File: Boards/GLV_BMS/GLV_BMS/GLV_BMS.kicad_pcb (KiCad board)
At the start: 2 copper layers, 44 parts, among them J1 CONN_02X03, J2 CONN_02X03, J3 MM_F_RA_20, U1 MCP2561-E_SN, U101 TPS560430YF, U2 ATMEGA16M1, U3 ATmega328P-AU, Y1 Crystal_SMD, Y2 Crystal_SMD

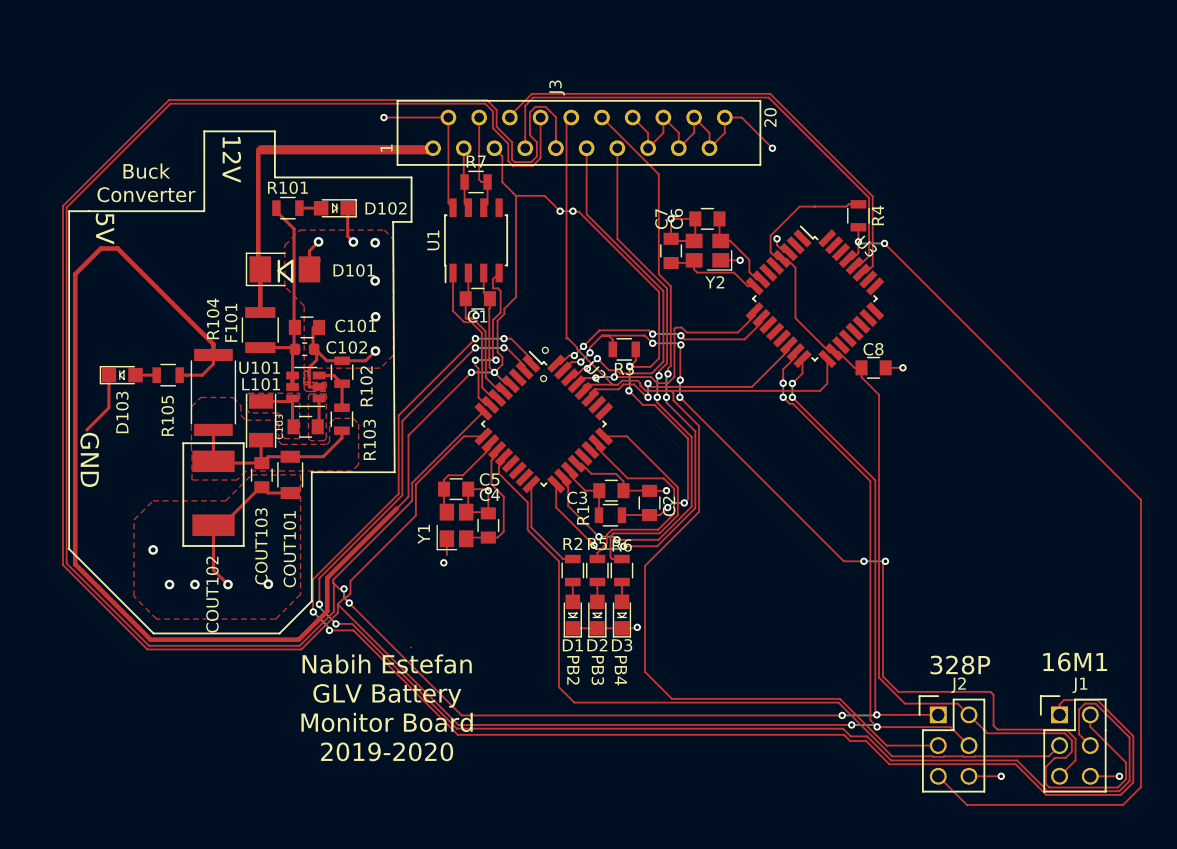
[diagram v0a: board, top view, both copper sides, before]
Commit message: Layout V4.0, added groundplane back (oops), reduced number of vias used, added more silk for understanding board
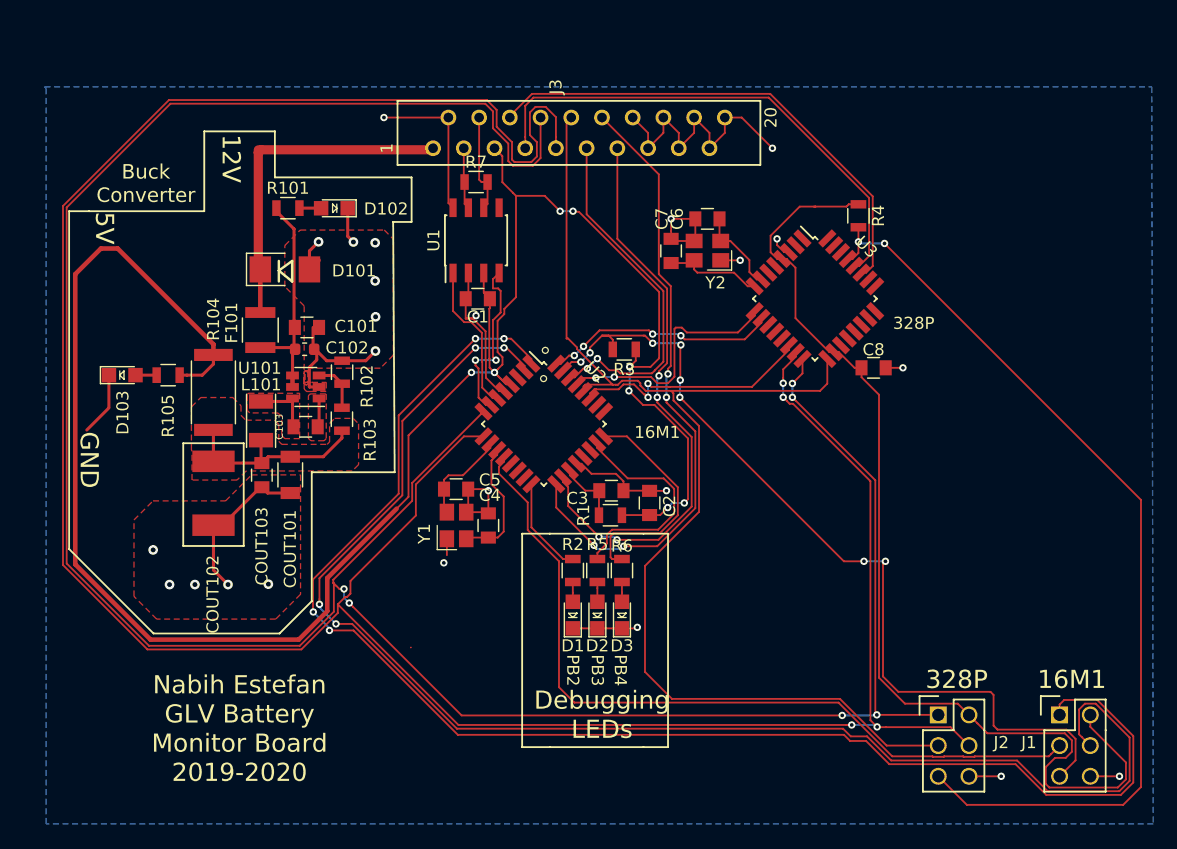
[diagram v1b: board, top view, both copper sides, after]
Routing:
- added copper zone on B.Cu, net GND
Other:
- board text added: "Debugging LEDs"
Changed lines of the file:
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@@
   (general
     (thickness 1.6)
-    (drawings 39)
+    (drawings 50)
     (tracks 782)
     (zones 0)
@@
     (34 B.Paste user)
     (35 F.Paste user)
-    (36 B.SilkS user hide)
+    (36 B.SilkS user)
     (37 F.SilkS user)
     (38 B.Mask user)
@@
     (descr "Through hole pin header")
     (tags "pin header")
-    (fp_text reference J2 (at 1.778 -2.54) (layer F.SilkS)
+    (fp_text reference J2 (at 5.207 2.286) (layer F.SilkS)
       (effects (font (size 1 1) (thickness 0.15)))
     )
@@
     (descr "Through hole pin header")
     (tags "pin header")
-    (fp_text reference J1 (at 1.778 -2.54) (layer F.SilkS)
+    (fp_text reference J1 (at -2.54 2.286) (layer F.SilkS)
       (effects (font (size 1 1) (thickness 0.15)))
     )
@@
     )
   )
-  (gr_text "328P\n" (at 174.625 122.809) (layer F.SilkS)
+  (gr_text 328P (at 170.815 94.488) (layer F.SilkS)
+    (effects (font (size 1 1) (thickness 0.15)))
+  )
+  (gr_text "16M1\n" (at 149.606 103.505) (layer F.SilkS)
+    (effects (font (size 1 1) (thickness 0.15)))
+  )
+  (gr_line (start 138.43 111.887) (end 140.716 111.887) (layer F.SilkS) (width 0.15))
+  (gr_line (start 138.43 129.54) (end 138.43 111.887) (layer F.SilkS) (width 0.15))
+  (gr_line (start 140.716 129.54) (end 138.43 129.54) (layer F.SilkS) (width 0.15))
+  (gr_line (start 150.495 129.54) (end 148.463 129.54) (layer F.SilkS) (width 0.15))
+  (gr_line (start 150.495 111.887) (end 150.495 129.54) (layer F.SilkS) (width 0.15))
+  (gr_line (start 148.463 111.887) (end 150.495 111.887) (layer F.SilkS) (width 0.15))
+  (gr_line (start 148.463 129.54) (end 140.716 129.54) (layer F.SilkS) (width 0.15))
+  (gr_text "Debugging \nLEDs" (at 145.034 126.873) (layer F.SilkS)
     (effects (font (size 1.5 1.5) (thickness 0.3)))
   )
-  (gr_text 16M1 (at 184.15 122.555) (layer F.SilkS)
+  (gr_line (start 140.716 111.887) (end 148.463 111.887) (layer F.SilkS) (width 0.15))
+  (gr_text "328P\n" (at 174.371 123.952) (layer F.SilkS)
+    (effects (font (size 1.5 1.5) (thickness 0.3)))
+  )
+  (gr_text 16M1 (at 183.896 123.952) (layer F.SilkS)
     (effects (font (size 1.5 1.5) (thickness 0.3)))
   )
@@
   (gr_line (start 185.42 74.93) (end 186.499999 74.93) (layer Dwgs.User) (width 0.2))
   (gr_line (start 185.42 74.93) (end 185.42 71.12) (layer Dwgs.User) (width 0.2))
-  (gr_text "Nabih Estefan\nGLV Battery\nMonitor Board\n2019-2020\n" (at 127.254 126.365) (layer F.SilkS)
+  (gr_text "Nabih Estefan\nGLV Battery\nMonitor Board\n2019-2020\n" (at 115.062 128.016) (layer F.SilkS)
     (effects (font (size 1.5 1.5) (thickness 0.3)))
   )
@@
   (segment (start 116.72886 89.98266) (end 116.7765 90.0303) (width 0.381) (layer F.Cu) (net 23))
   (segment (start 116.60886 89.86266) (end 116.7765 90.0303) (width 0.381) (layer F.Cu) (net 23))
-  (segment (start 116.60886 80.36814) (end 116.60886 89.86266) (width 0.381) (layer F.Cu) (net 23))
+  (segment (start 116.60886 80.36814) (end 116.60886 89.86266) (width 0.762) (layer F.Cu) (net 23))
   (segment (start 116.84 80.137) (end 130.683 80.137) (width 0.762) (layer F.Cu) (net 23))
-  (segment (start 116.60886 80.36814) (end 116.84 80.137) (width 0.1524) (layer F.Cu) (net 23))
-  (segment (start 116.60886 80.144378) (end 116.60886 80.36814) (width 0.381) (layer F.Cu) (net 23))
+  (segment (start 116.60886 80.36814) (end 116.84 80.137) (width 0.762) (layer F.Cu) (net 23))
+  (segment (start 116.60886 80.144378) (end 116.60886 80.36814) (width 0.762) (layer F.Cu) (net 23))
   (segment (start 135.0676 82.804) (end 135.57 82.804) (width 0.1524) (layer F.Cu) (net 24))
   (segment (start 134.874 82.6104) (end 135.0676 82.804) (width 0.1524) (layer F.Cu) (net 24))
@@
       )
     )
+  )
+  (zone (net 1) (net_name GND) (layer B.Cu) (hatch edge 0.508)
+    (connect_pads (clearance 0.1524))
+    (min_thickness 0.254)
+    (fill yes (arc_segments 32) (thermal_gap 0.508) (thermal_bridge_width 0.508))
+    (polygon
+      (pts
+        (xy 190.627 135.89) (xy 99.06 135.89) (xy 99.06 75.057) (xy 98.933 74.93) (xy 190.5 74.93)
+      )
+    )

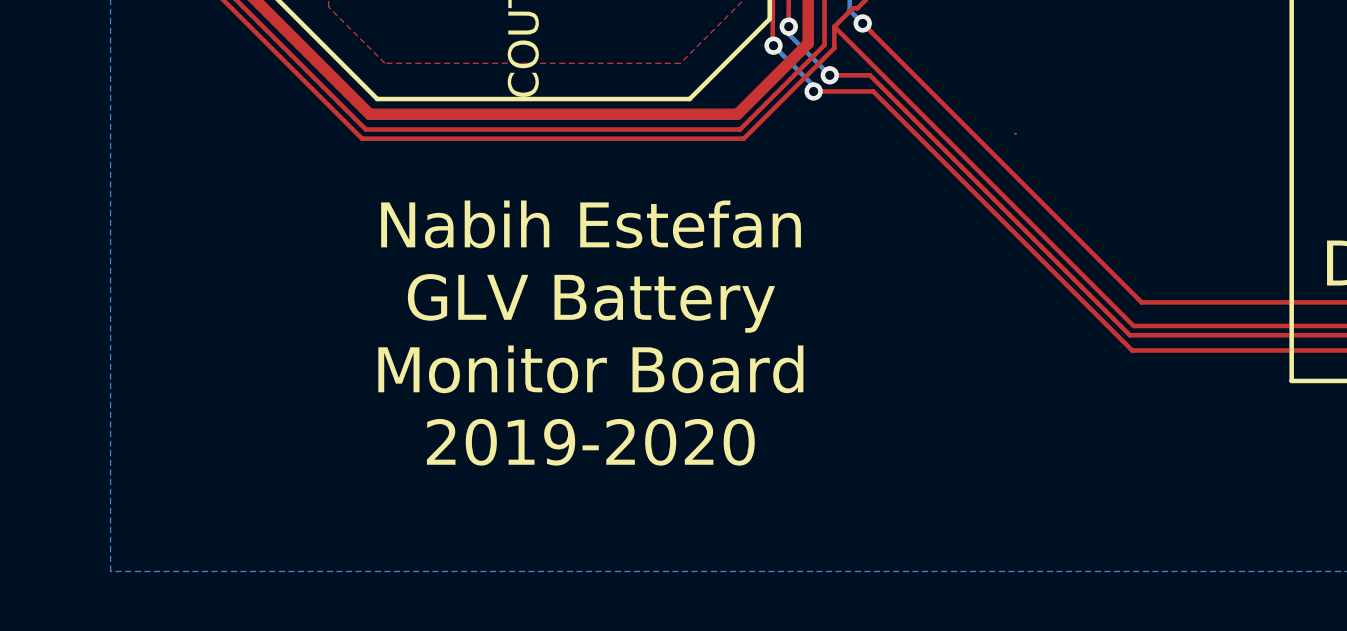
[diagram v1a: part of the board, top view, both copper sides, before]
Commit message: created BOM for board
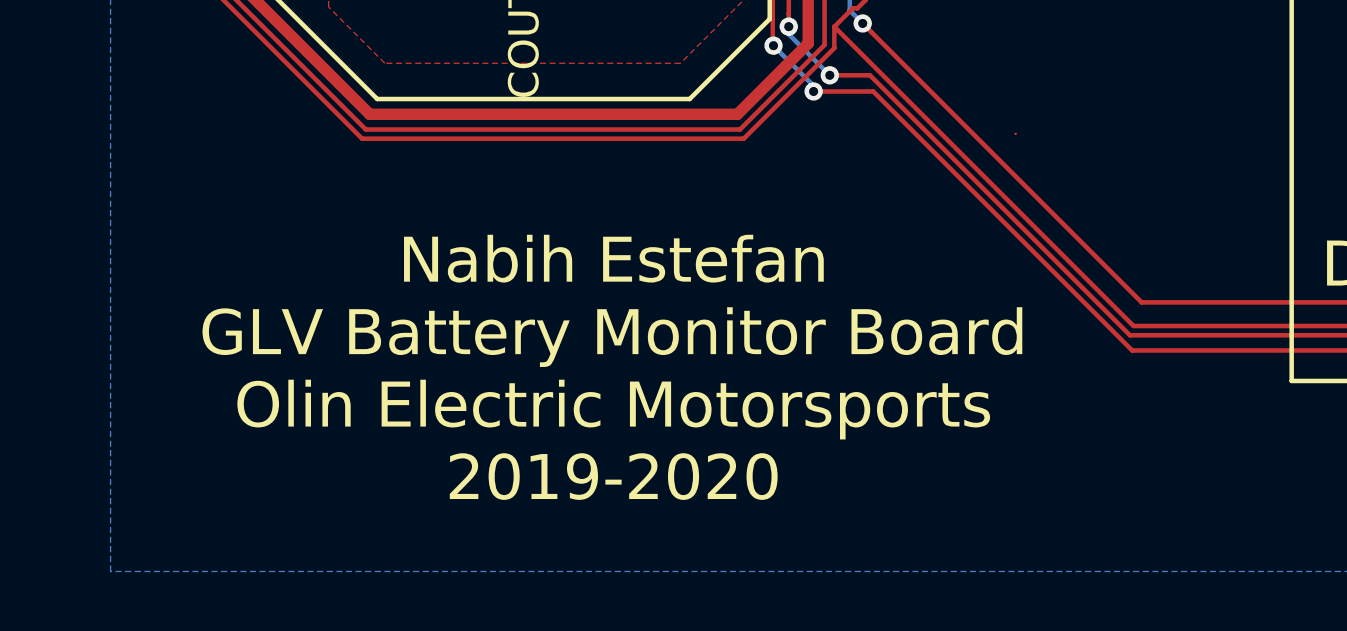
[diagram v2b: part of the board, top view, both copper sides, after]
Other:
- board text added: "Nabih Estefan GLV Battery Monitor Board Olin Electric Motorsports 2019-2020"
- board text removed: "Nabih Estefan GLV Battery Monitor Board 2019-2020"
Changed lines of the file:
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@@
     (solder_mask_min_width 0.25)
     (aux_axis_origin 0 0)
-    (visible_elements FFFFFF7F)
+    (visible_elements FFFFF77F)
     (pcbplotparams
       (layerselection 0x010fc_ffffffff)
@@
   (gr_line (start 185.42 74.93) (end 186.499999 74.93) (layer Dwgs.User) (width 0.2))
   (gr_line (start 185.42 74.93) (end 185.42 71.12) (layer Dwgs.User) (width 0.2))
-  (gr_text "Nabih Estefan\nGLV Battery\nMonitor Board\n2019-2020\n" (at 115.062 128.016) (layer F.SilkS)
+  (gr_text "Nabih Estefan\nGLV Battery Monitor Board\nOlin Electric Motorsports\n2019-2020\n" (at 115.824 129.159) (layer F.SilkS)
     (effects (font (size 1.5 1.5) (thickness 0.3)))
   )
@@
     (connect_pads (clearance 0.1524))
     (min_thickness 0.254)
-    (fill yes (arc_segments 32) (thermal_gap 0.508) (thermal_bridge_width 0.508))
+    (fill (arc_segments 32) (thermal_gap 0.508) (thermal_bridge_width 0.508))
     (polygon
       (pts

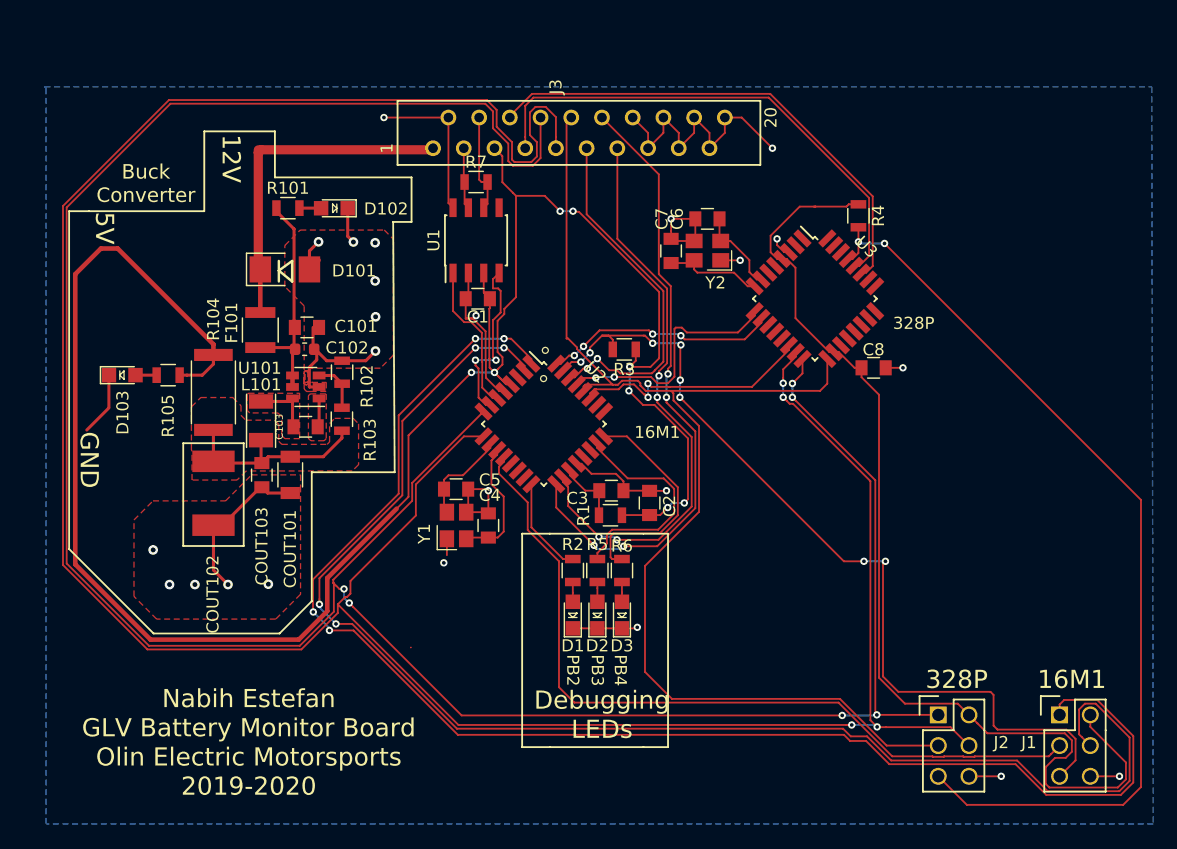
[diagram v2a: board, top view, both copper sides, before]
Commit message: made changes to coding pins, saving before turning other pin
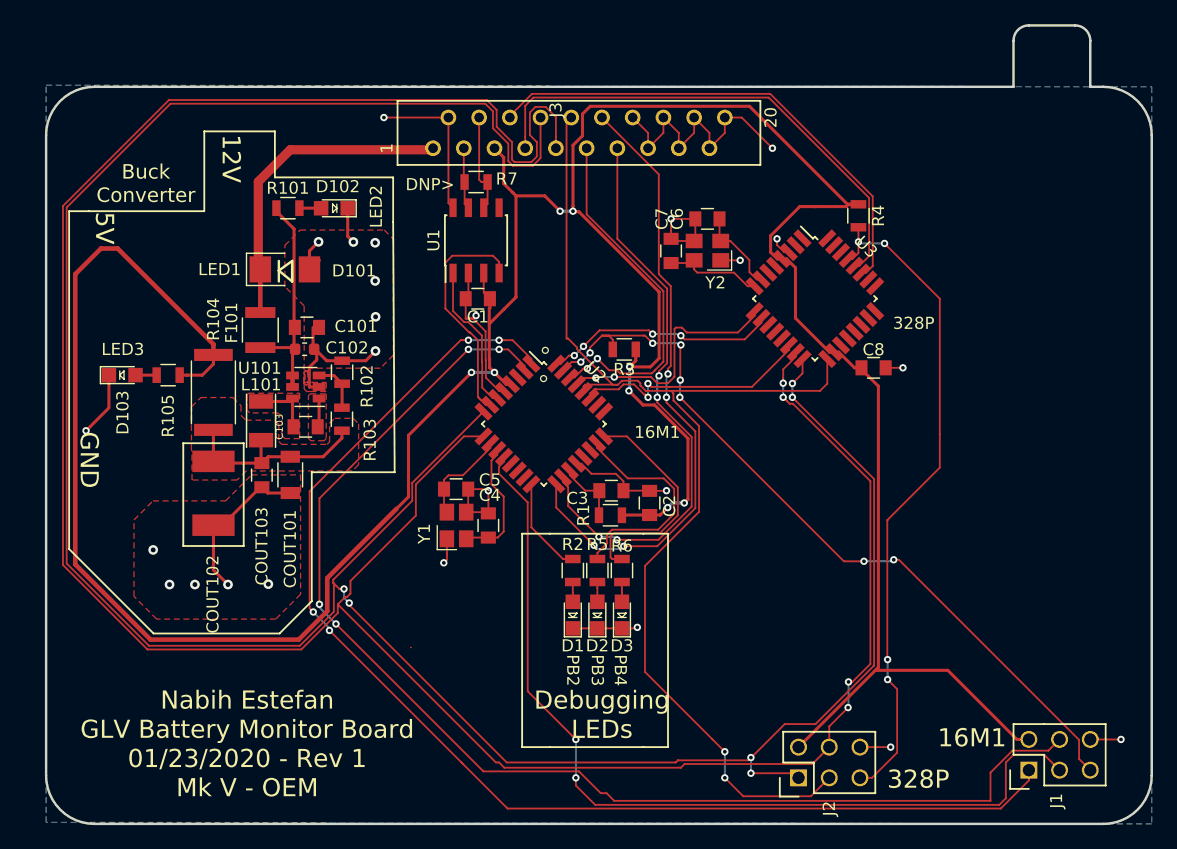
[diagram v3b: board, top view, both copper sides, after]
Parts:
- moved J2 12.7 mm to (161.3, 132.1), turned to 90 degrees
- moved J1 5.23 mm to (180.3, 131.4), turned to 90 degrees
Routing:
- net /RESET_2: track 77.5 -> 55.5 mm, vias 2 -> 4
- net /MISO: track 120.7 -> 102.7 mm
- net VCC: track 259.4 -> 276.5 mm
- net /MOSI: track 118.0 -> 103.4 mm
- net /SCK: track 65.5 -> 74.6 mm, vias 0 -> 2
- net /RESET: track 73.2 -> 65.5 mm
- net /MOSI_2: track 224.8 -> 217.9 mm
- net /CAN_RX: track 14.4 -> 20.2 mm, vias 2 -> 0
- net /SCK_2: track 100.8 -> 95.5 mm, vias 0 -> 2
- net +12V: track 27.8 -> 26.1 mm
- net /MISO_2: track 215.1 -> 216.1 mm
- net GND: track 126.7 -> 127.7 mm, vias 24 -> 25
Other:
- board outline added: 91.4 x 66 mm
- board text added: "DNP>"
- board text added: "LED1"
- board text added: "LED2"
- board text added: "LED3"
- board text added: "Nabih Estefan GLV Battery Monitor Board 01/23/2020 - Rev 1 Mk V - OEM"
- board text removed: "Nabih Estefan GLV Battery Monitor Board Olin Electric Motorsports 2019-2020"

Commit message: Turned pins around and fixed board. Finished Rev 2.
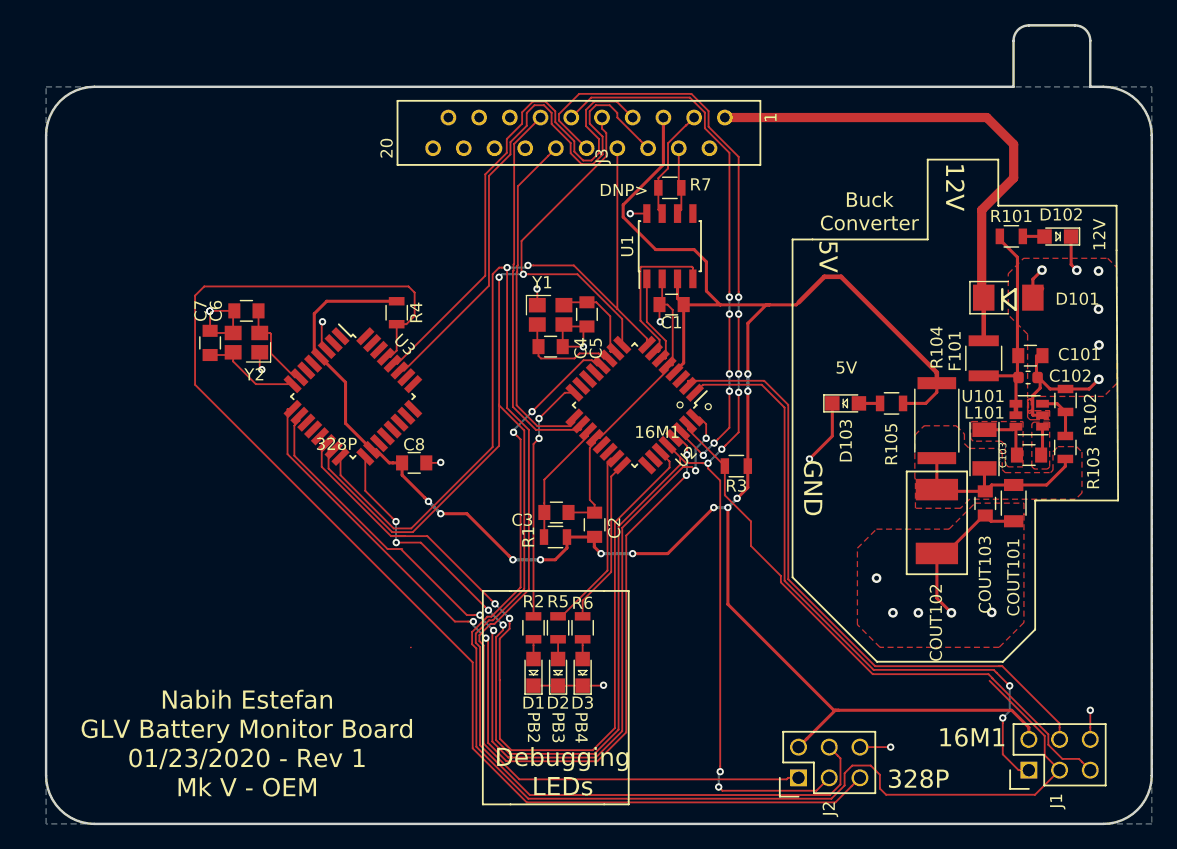
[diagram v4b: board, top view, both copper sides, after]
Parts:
- moved COUT103 59.9 mm to (176.7, 109.4)
- moved D101 59.9 mm to (178.6, 92.4)
- moved R103 59.9 mm to (183.4, 104.8)
- moved C102 59.9 mm to (180.3, 99.0)
- moved C103 59.9 mm to (180.4, 105.4)
- moved D102 59.9 mm to (182.7, 87.3)
- moved F101 59.9 mm to (176.6, 97.4)
- moved L101 59.9 mm to (176.7, 104.9)
- moved R101 59.9 mm to (178.9, 87.3)
- moved R104 59.9 mm to (172.7, 102.5)
- moved R105 59.9 mm to (169.0, 101.1)
- moved C101 59.9 mm to (180.5, 97.2)
- moved COUT101 59.9 mm to (179.1, 109.4)
- moved COUT102 59.9 mm to (172.7, 108.2)
- moved D103 59.9 mm to (165.2, 101.1)
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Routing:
- net VCC: track 276.5 -> 179.6 mm, vias 8 -> 11
- net /MOSI_2: track 217.9 -> 131.5 mm, vias 4 -> 2
- net /MISO_2: track 216.1 -> 131.9 mm, vias 6 -> 2
- net /SCK_2: track 95.5 -> 155.2 mm, vias 2 -> 12
- net /INFO2: track 19.4 -> 78.2 mm
- net /INFO1: track 20.5 -> 75.9 mm, vias 2 -> 4
- net /RESET_2: track 55.5 -> 107.4 mm, vias 4 -> 0
- net /MOSI: track 103.4 -> 52.7 mm, vias 4 -> 0
- net /CS_2: track 21.0 -> 70.2 mm
- net /MISO: track 102.7 -> 53.6 mm, vias 4 -> 2
- net GND: track 127.7 -> 98.4 mm, vias 25 -> 24
- net /SCK: track 74.6 -> 102.3 mm
- net /ALERT_GLV: track 52.1 -> 28.6 mm, vias 4 -> 0
- net /RESET: track 65.5 -> 48.9 mm, vias 8 -> 0
- net /ALERT_COOLING: track 47.9 -> 31.7 mm, vias 4 -> 0
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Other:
- board text removed: "LED1"
- board text removed: "LED2"
- board text removed: "LED3"
